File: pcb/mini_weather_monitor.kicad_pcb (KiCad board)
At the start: 2 copper layers, 135 x 72 mm, 25 parts, among them J1 Conn_01x02, Q1 IRLML6402, U2 4.0inch_SPI_MSP4021, U2_BME280 module_bme280, U3_BH1750 module_bh1750

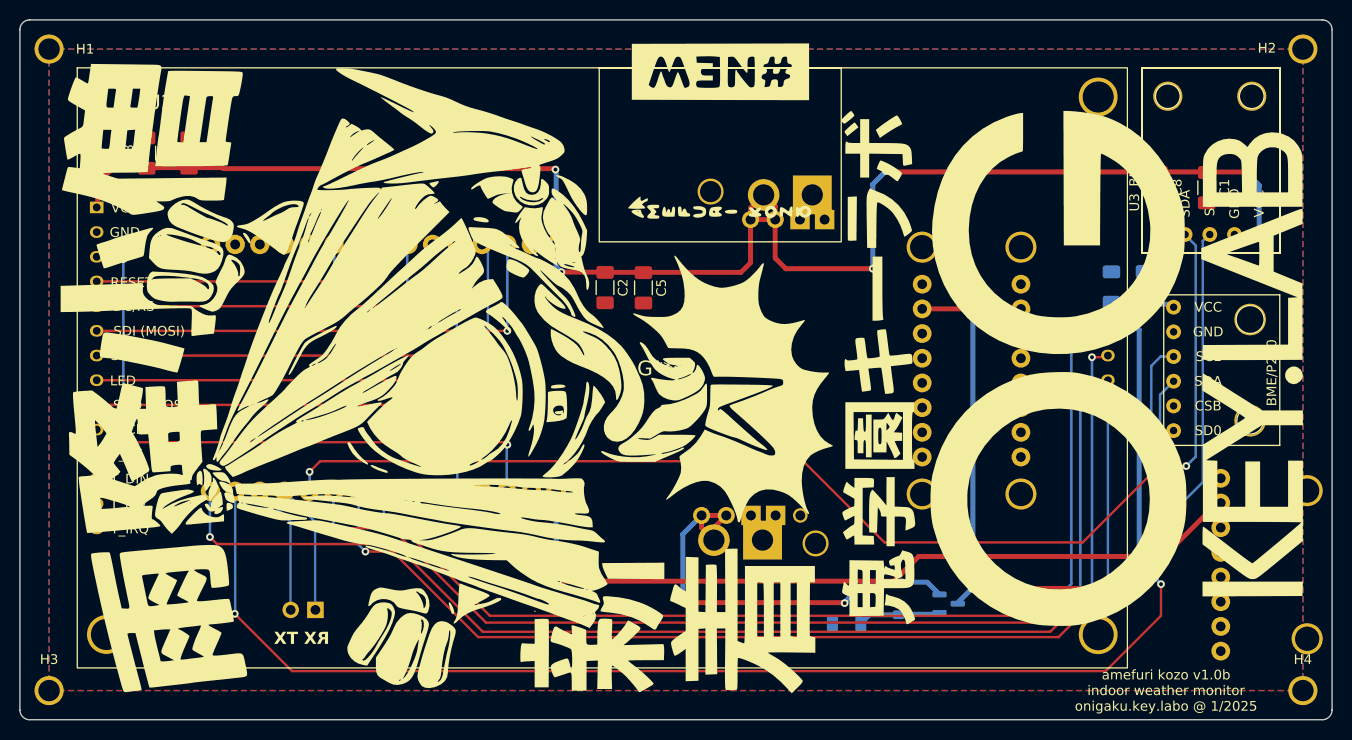
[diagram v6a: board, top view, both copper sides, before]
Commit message: adding mini sdcard to use instead of onboard sdcard
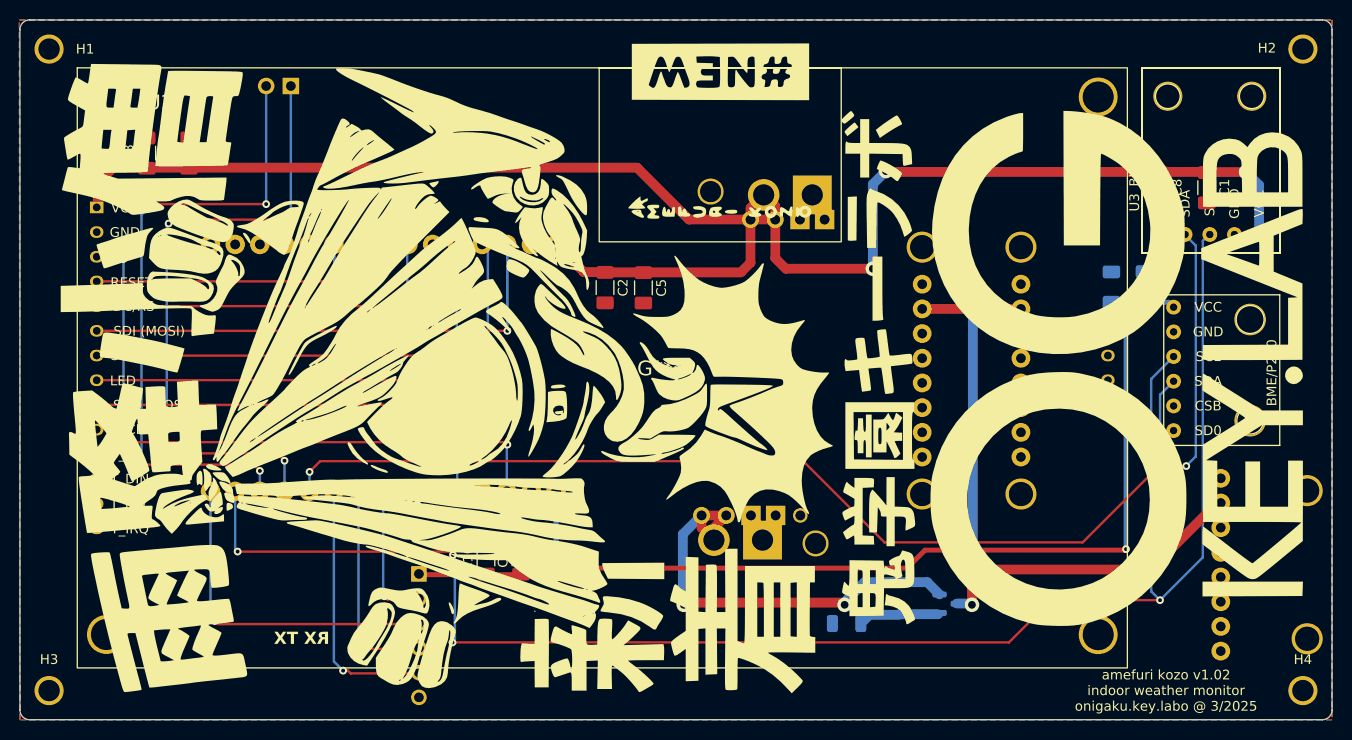
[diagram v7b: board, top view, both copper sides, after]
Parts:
- added C10: 100nF, Capacitor_SMD:C_1206_3216Metric_Pad1.33x1.80mm_HandSolder, F.Cu at (114.0, 119.5)
- added C9: 10uF, Capacitor_SMD:C_1206_3216Metric_Pad1.33x1.80mm_HandSolder, F.Cu at (117.5, 119.5)
- added U3_minisdcard1: ~, mini_weather_monitor:zicheng_mini_sd_card_reader, B.Cu at (99.0, 127.0)
- moved J1 54.0 mm to (93.9, 70.8)
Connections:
- U2 pad 15: Net-(U2-SD_CS) -> unconnected-(U2-SD_CS-Pad15)
- U2 pad 16: Net-(U2-SD_MOSI) -> unconnected-(U2-SD_MOSI-Pad16)
- U2 pad 17: Net-(U2-SD_MISO) -> unconnected-(U2-SD_MISO-Pad17)
- U2 pad 18: Net-(U2-SD_SCK) -> unconnected-(U2-SD_SCK-Pad18)
- U_ESP32_DEVKIT_V1 pad 10: Net-(U2-SD_MISO) -> Net-(U3_minisdcard1-MISO)
- U_ESP32_DEVKIT_V1 pad 15: Net-(U2-SD_MOSI) -> Net-(U3_minisdcard1-MOSI)
- U_ESP32_DEVKIT_V1 pad 8: Net-(U2-SD_CS) -> Net-(U3_minisdcard1-CS)
- U_ESP32_DEVKIT_V1 pad 9: Net-(U2-SD_SCK) -> Net-(U3_minisdcard1-CLK)
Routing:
- net Net-(U2-SD_MOSI): track 127.4 -> 0.00 mm, vias 3 -> 0
- net Net-(U2-SD_MISO): track 110.3 -> 0.00 mm, vias 3 -> 0
- net Net-(U2-SD_SCK): track 108.1 -> 0.00 mm, vias 2 -> 0
- net Net-(U2-SD_CS): track 108.0 -> 0.00 mm, vias 3 -> 0
- net Net-(J1-Pin_2): track 13.5 -> 65.7 mm, vias 0 -> 4
- net Net-(J1-Pin_1): track 13.5 -> 65.4 mm, vias 0 -> 4
- net Net-(U3_minisdcard1-MOSI): track 0.00 -> 34.7 mm, vias 0 -> 1
- net Net-(U3_minisdcard1-MISO): track 0.00 -> 26.8 mm, vias 0 -> 1
- net Net-(U3_minisdcard1-CLK): track 0.00 -> 22.0 mm, vias 0 -> 1
- net Net-(U3_minisdcard1-CS): track 0.00 -> 14.6 mm, vias 0 -> 1
- net VCC: track 163.7 -> 177.8 mm, vias 5 -> 3
- net +3V3: track 103.3 -> 114.5 mm
- net Net-(Q1-D): track 71.4 -> 74.1 mm
- net Net-(U2_BME280-SCL): track 179.9 -> 178.5 mm, vias 2 -> 4
- net VBUS: track 46.3 -> 47.0 mm
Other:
- board text added: "amefuri kozo v1.02 indoor weather monitor onigaku.key.labo @ 3/2025"
- board text removed: "amefuri kozo v1.0b indoor weather monitor onigaku.key.labo @ 1/2025"

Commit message: moved config info to config on sdcard
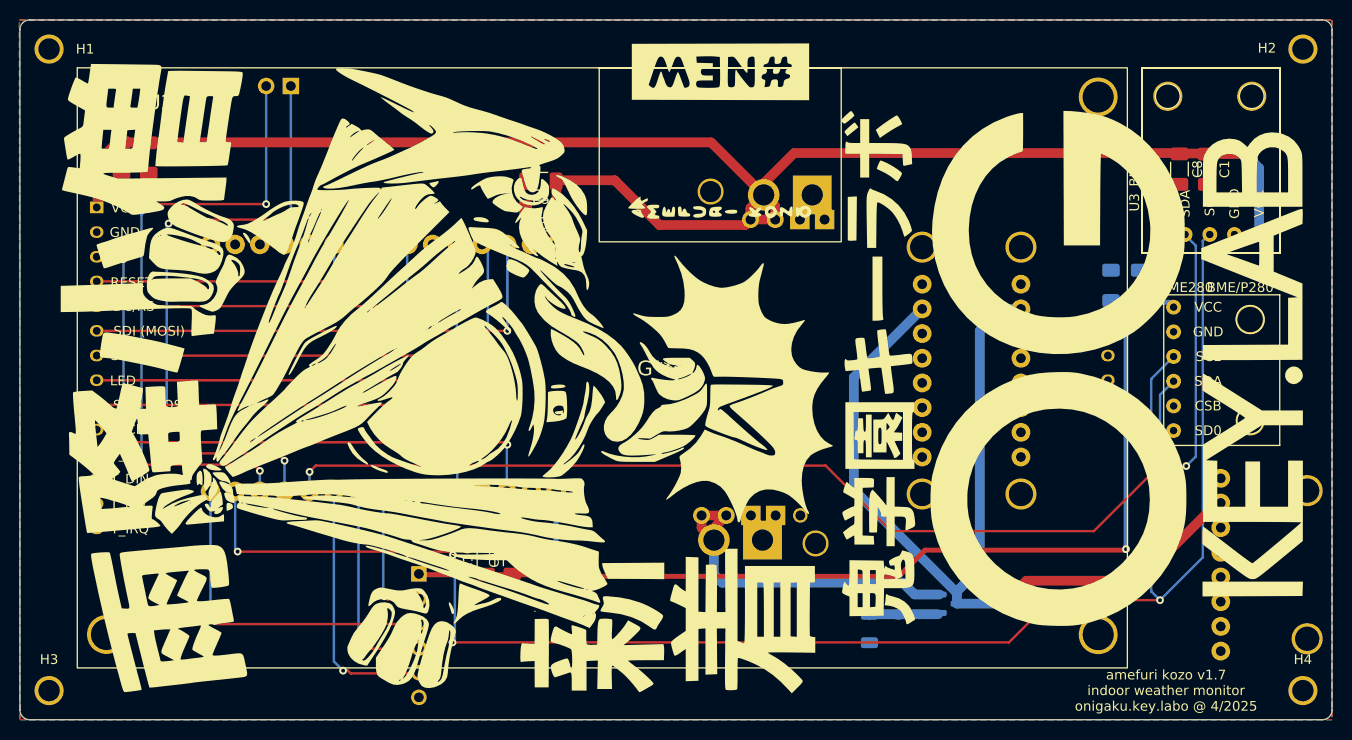
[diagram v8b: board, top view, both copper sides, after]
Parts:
- U2_BME280: value module_bme280 -> bme280
- U3_BH1750: value module_bh1750 -> bh1750
- moved C5 15.2 mm to (119.6, 80.6), turned to 180 degrees
- moved C2 10.4 mm to (119.6, 83.5), turned to 180 degrees
- moved C6 4.18 mm to (79.2, 78.2), turned to -90 degrees
- moved C7 3.45 mm to (178.2, 91.3)
- moved C4 2.91 mm to (181.2, 91.3)
- moved C8 2.83 mm to (185.3, 79.3)
- moved C3 2.65 mm to (76.5, 78.2), turned to -90 degrees
- moved R2 2.41 mm to (153.4, 126.6), turned to -90 degrees
- moved C1 1.90 mm to (188.1, 79.4)
- moved C9 0.90 mm to (116.7, 119.5)
- renumbered U1 to boost_converter
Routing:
- net Net-(Q1-D): track 74.1 -> 103.2 mm, vias 2 -> 1
- net VBUS: track 47.0 -> 36.3 mm, vias 2 -> 0
- net VCC: track 177.8 -> 179.5 mm, vias 3 -> 1
- net Net-(U2_BME280-SDA): track 133.4 -> 132.1 mm
- net Net-(D1-A): track 8.55 -> 7.32 mm
- net +3V3: track 114.5 -> 115.2 mm
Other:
- board text added: "amefuri kozo v1.7 indoor weather monitor onigaku.key.labo @ 4/2025"
- board text removed: "amefuri kozo v1.02 indoor weather monitor onigaku.key.labo @ 3/2025"
